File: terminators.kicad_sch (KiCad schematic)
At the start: 13 parts, among them U37 74LS32

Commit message: DRAM chips replaced with SIMM module
Added logic to decode 2MB chip + 1.5MB slow
Rewired trapdoor slot
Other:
- title: Rämixx500 -> Rämixx500_max
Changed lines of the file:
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@@
 	(paper "A4")
 	(title_block
-		(title "Rämixx500")
-		(date "2021-05-16")
-		(rev "1")
+		(title "Rämixx500_max")
+		(date "2026-03-13")
+		(rev "2")
 		(company "SukkoPera")
 		(comment 4 "Licensed under CC BY-NC-SA 4.0")

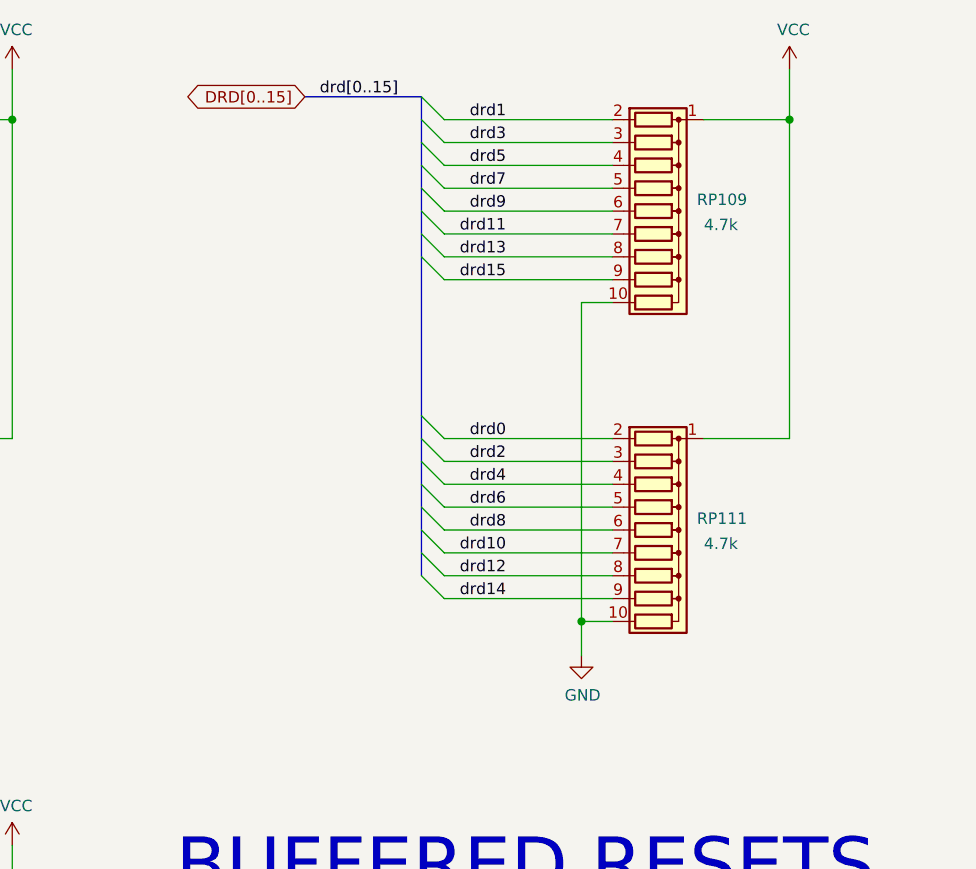
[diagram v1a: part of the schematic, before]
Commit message: routing SIMM
work in progress
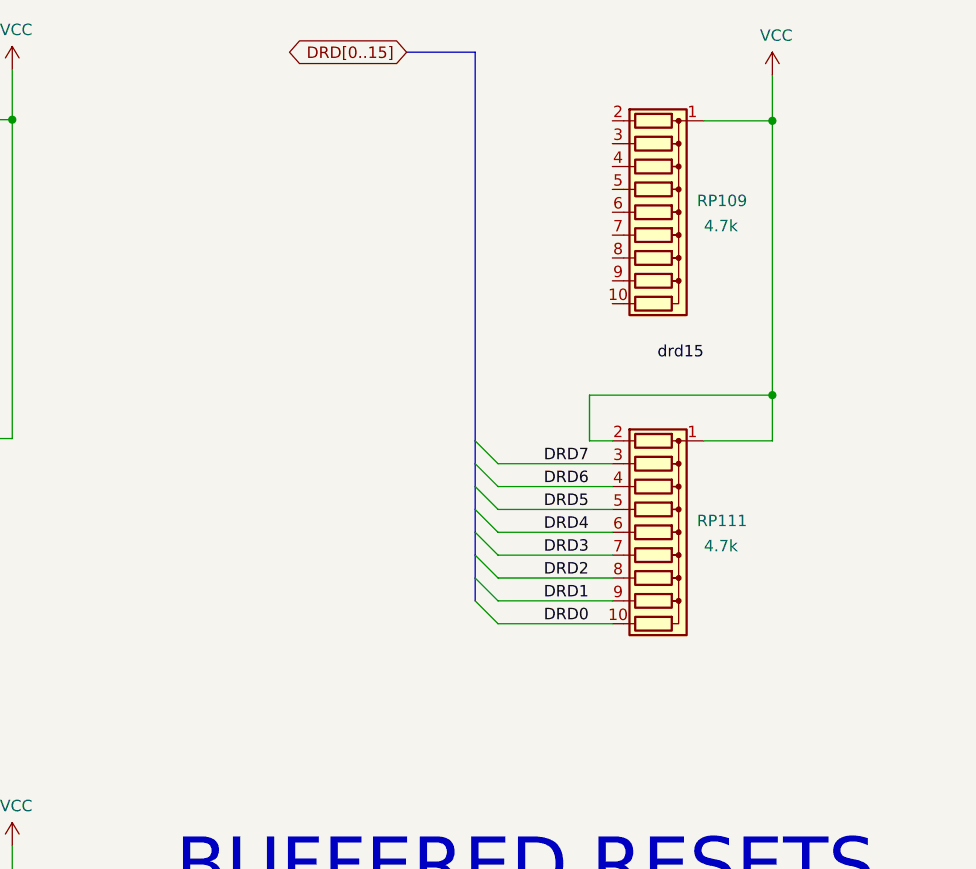
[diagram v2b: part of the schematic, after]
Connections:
- net drd0 is gone; now on net VCC: RP111.2 (R1)
- net GND: no longer RP109.10 (R9), RP111.10 (R9)
- net drd15: no longer RP109.9 (R8)
- net drd1: no longer names the net of RP109.2 (R1)
- net drd10 renamed DRD3
- net drd11: no longer names the net of RP109.7 (R6)
- net drd12 renamed DRD2
- net drd13: no longer names the net of RP109.8 (R7)
- net drd14 renamed DRD1
- net drd2 renamed DRD7
- net drd3: no longer names the net of RP109.3 (R2)
- net drd4 renamed DRD6
- net drd5: no longer names the net of RP109.4 (R3)
- net drd6 renamed DRD5
- net drd7: no longer names the net of RP109.5 (R4)
- net drd8 renamed DRD4
- net drd9: no longer names the net of RP109.6 (R5)
- new net DRD0: RP111.10 (R9)

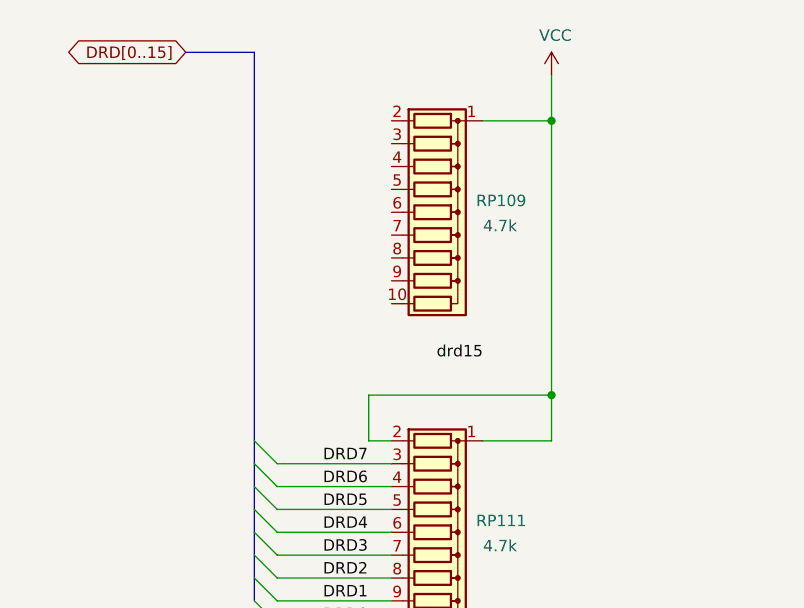
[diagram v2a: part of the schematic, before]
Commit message: changed wiring of pullups, simplified SIMM parity pullups
Routed more nets. Slowly getting there. WIP
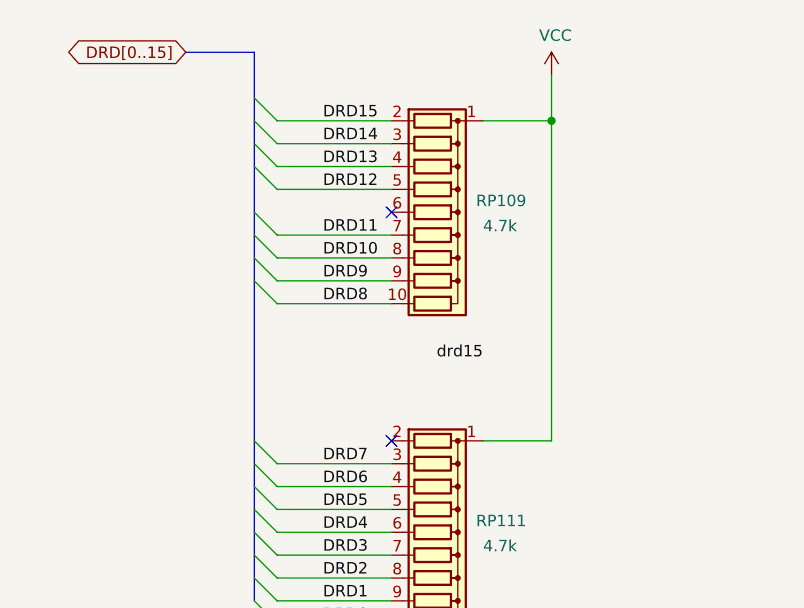
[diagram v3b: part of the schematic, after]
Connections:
- net VCC: no longer RP111.2 (R1)
- net DRD8: now reaches RP109.10 (R9)
- net DRD15: now reaches RP109.2 (R1)
- net DRD14: now reaches RP109.3 (R2)
- net DRD13: now reaches RP109.4 (R3)
- net DRD12: now reaches RP109.5 (R4)
- net DRD11: now reaches RP109.7 (R6)
- net DRD10: now reaches RP109.8 (R7)
- net DRD9: now reaches RP109.9 (R8)
- no-connect marks 4 -> 6

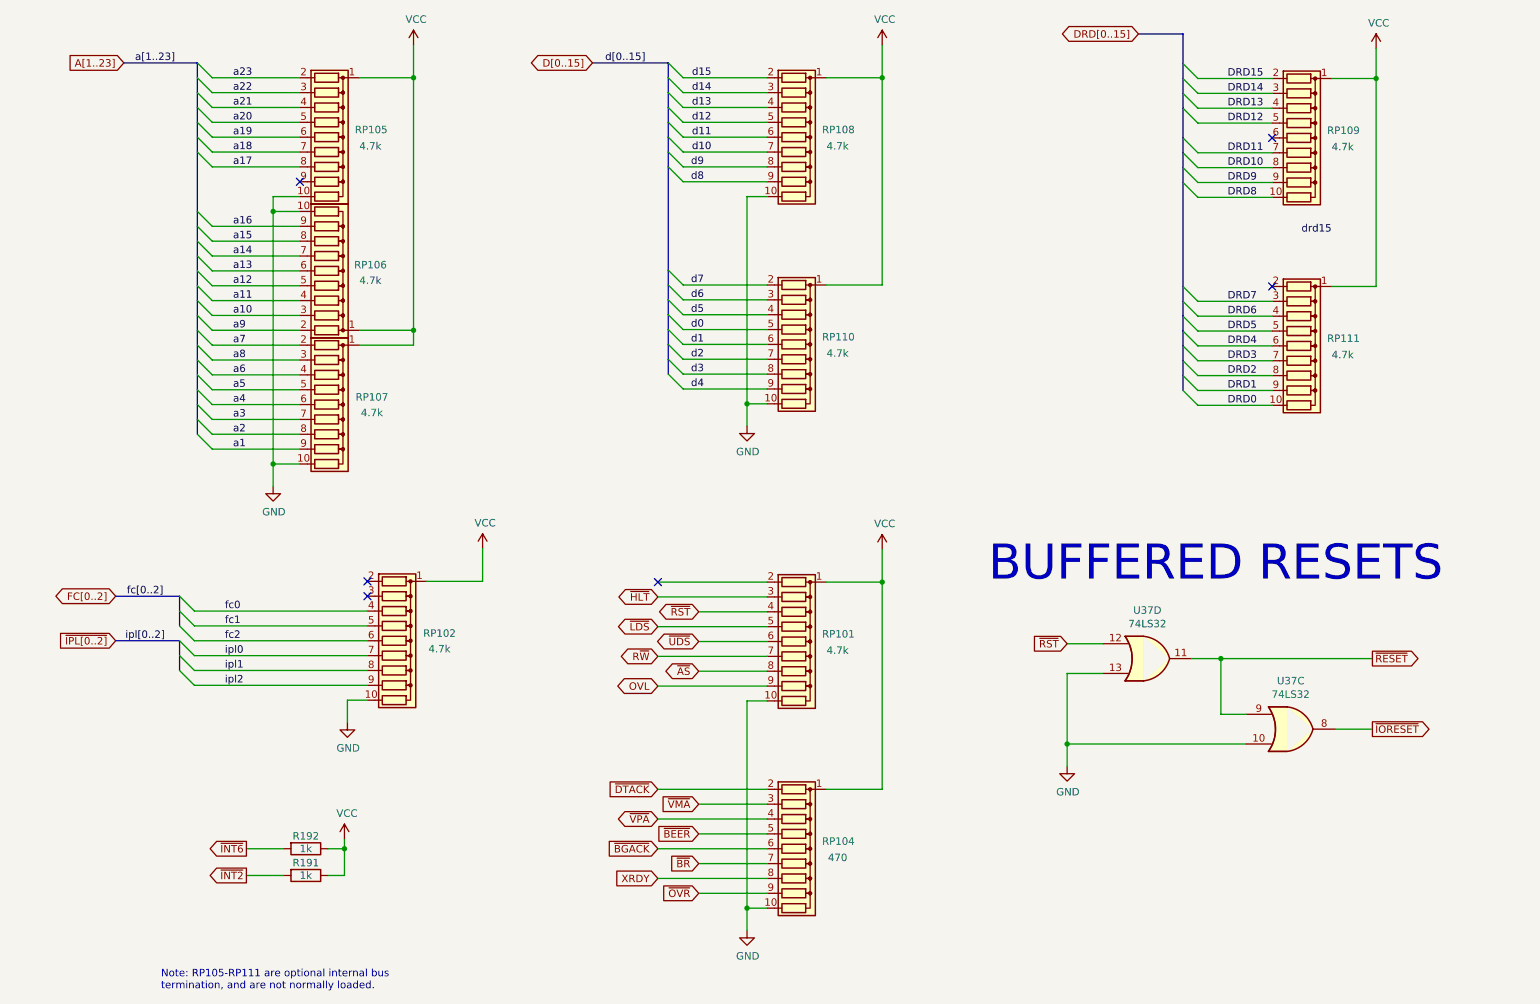
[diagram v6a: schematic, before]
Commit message: Started cleaning up BOM
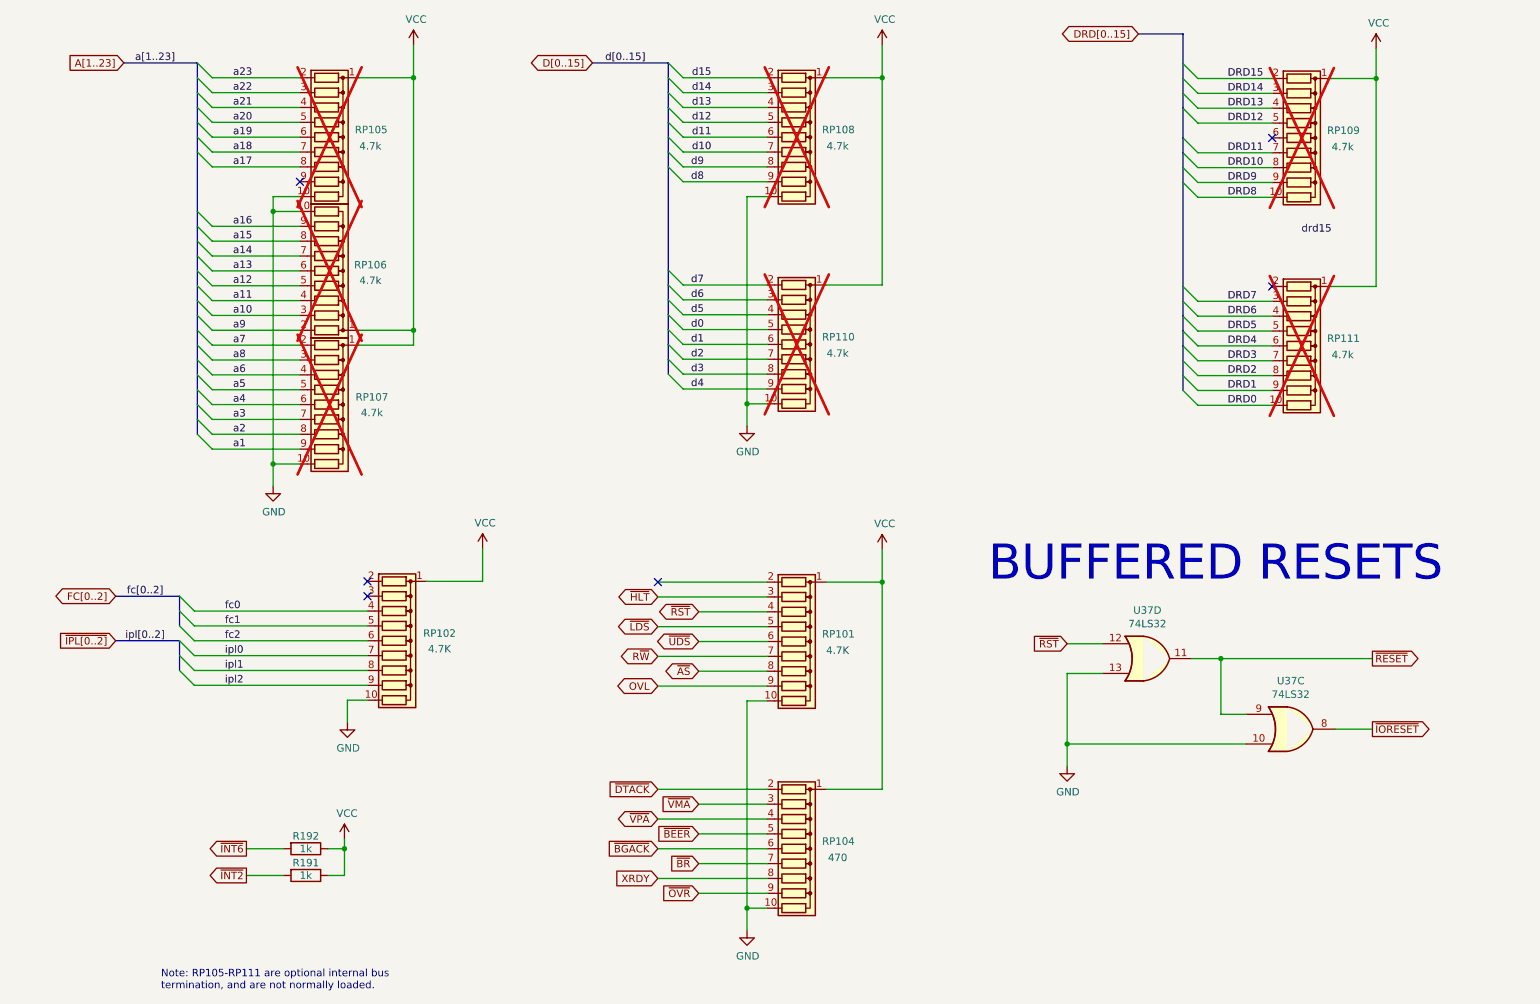
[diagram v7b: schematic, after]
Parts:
- RP101, RP102: value 4.7k -> 4.7K
- RP105, RP106, RP107, RP108, RP109, RP110, RP111: now not fitted
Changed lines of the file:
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@@
 		(in_bom yes)
 		(on_board yes)
-		(dnp no)
+		(dnp yes)
 		(property "Reference" "RP107"
 			(at 87.376 87.503 90)
@@
 		(in_bom yes)
 		(on_board yes)
-		(dnp no)
+		(dnp yes)
 		(property "Reference" "RP106"
 			(at 87.122 64.897 90)
@@
 		(in_bom yes)
 		(on_board yes)
-		(dnp no)
+		(dnp yes)
 		(property "Reference" "RP105"
 			(at 87.249 41.783 90)
@@
 		(in_bom yes)
 		(on_board yes)
-		(dnp no)
+		(dnp yes)
 		(property "Reference" "RP108"
 			(at 167.132 41.783 90)
@@
 		(in_bom yes)
 		(on_board yes)
-		(dnp no)
+		(dnp yes)
 		(property "Reference" "RP110"
 			(at 167.132 77.216 90)
@@
 		(in_bom yes)
 		(on_board yes)
-		(dnp no)
+		(dnp yes)
 		(property "Reference" "RP109"
 			(at 253.492 41.91 90)
@@
 		(in_bom yes)
 		(on_board yes)
-		(dnp no)
+		(dnp yes)
 		(property "Reference" "RP111"
 			(at 253.492 77.47 90)
@@
 			)
 		)
-		(property "Value" "4.7k"
+		(property "Value" "4.7K"
 			(at 98.933 130.556 90)
 			(effects
@@
 			)
 		)
-		(property "Value" "4.7k"
+		(property "Value" "4.7K"
 			(at 167.005 130.81 90)
 			(effects
